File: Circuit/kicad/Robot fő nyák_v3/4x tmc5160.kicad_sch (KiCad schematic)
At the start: 28 parts, among them M6 Stepper_Motor_unipolar_6pin, M7 Stepper_Motor_unipolar_6pin, M8 Stepper_Motor_unipolar_6pin, M9 Stepper_Motor_unipolar_6pin, U42 TMC2240_SILENTSTEPSTICK, U43 TMC2240_SILENTSTEPSTICK, U44 TMC2240_SILENTSTEPSTICK, U45 TMC2240_SILENTSTEPSTICK

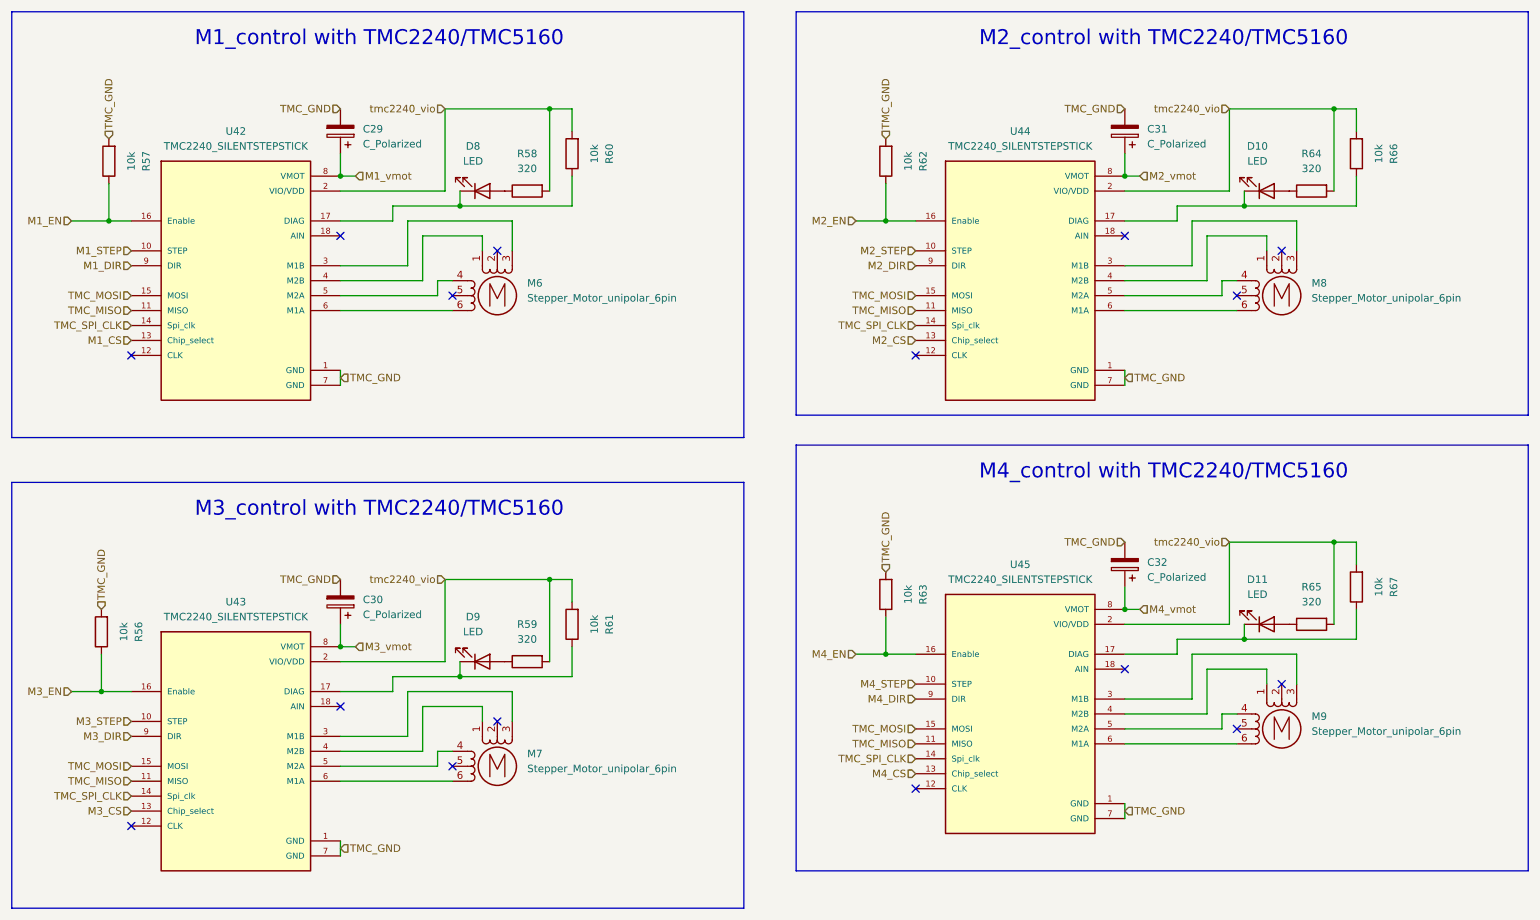
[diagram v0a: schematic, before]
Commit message: kicad i2c schematic updated: gyto i2c bugfixes, +add new datasheets
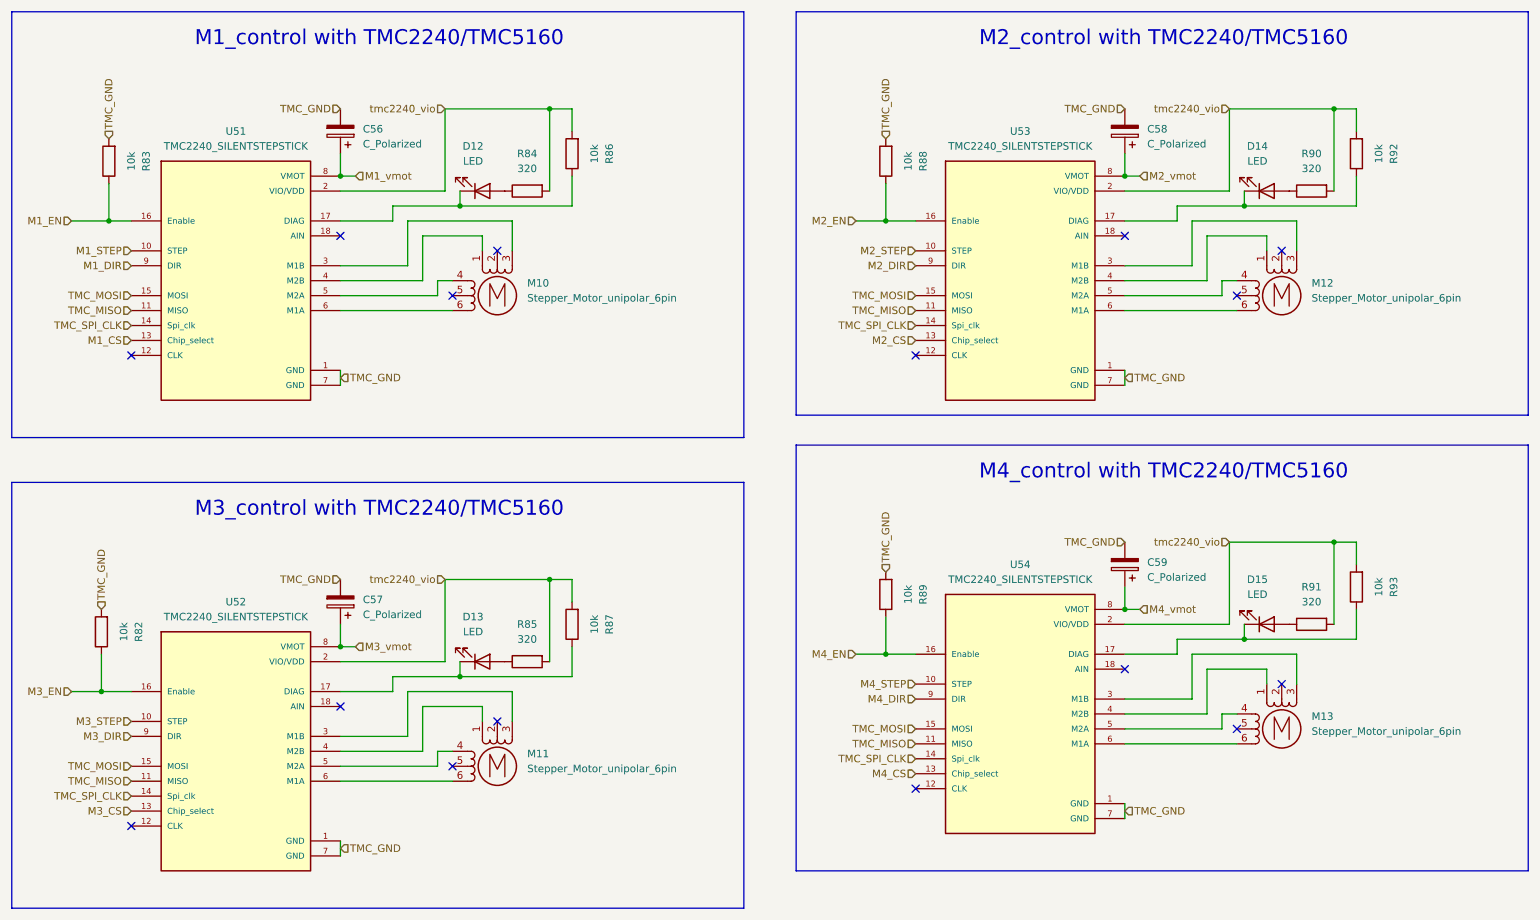
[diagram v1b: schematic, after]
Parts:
- M10: renamed from M6; footprint (none) -> Connector_JST:JST_PH_B6B-PH-K_1x06_P2.00mm_Vertical
- M11: renamed from M7; footprint (none) -> Connector_JST:JST_PH_B6B-PH-K_1x06_P2.00mm_Vertical
- M12: renamed from M8; footprint (none) -> Connector_JST:JST_PH_B6B-PH-K_1x06_P2.00mm_Vertical
- M13: renamed from M9; footprint (none) -> Connector_JST:JST_PH_B6B-PH-K_1x06_P2.00mm_Vertical
- renumbered C29 to C56, C30 to C57, C31 to C58, C32 to C59, D8 to D12, D9 to D13, D10 to D14, D11 to D15, R56 to R82, R57 to R83, R58 to R84, R59 to R85, R60 to R86, R61 to R87, R62 to R88, R63 to R89, R64 to R90, R65 to R91, R66 to R92, R67 to R93, U42 to U51, U43 to U52, U44 to U53, U45 to U54

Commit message: kicad bugfixs + bno085 + level shifter ics
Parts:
- U51: footprint fds:MODULE_TMC2209_SILENTSTEPSTICK -> CM5IO:TMC2209
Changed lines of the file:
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@@
 			)
 		)
-		(property "Footprint" "fds:MODULE_TMC2209_SILENTSTEPSTICK"
+		(property "Footprint" "CM5IO:TMC2209"
 			(at 62.992 27.686 0)
 			(effects

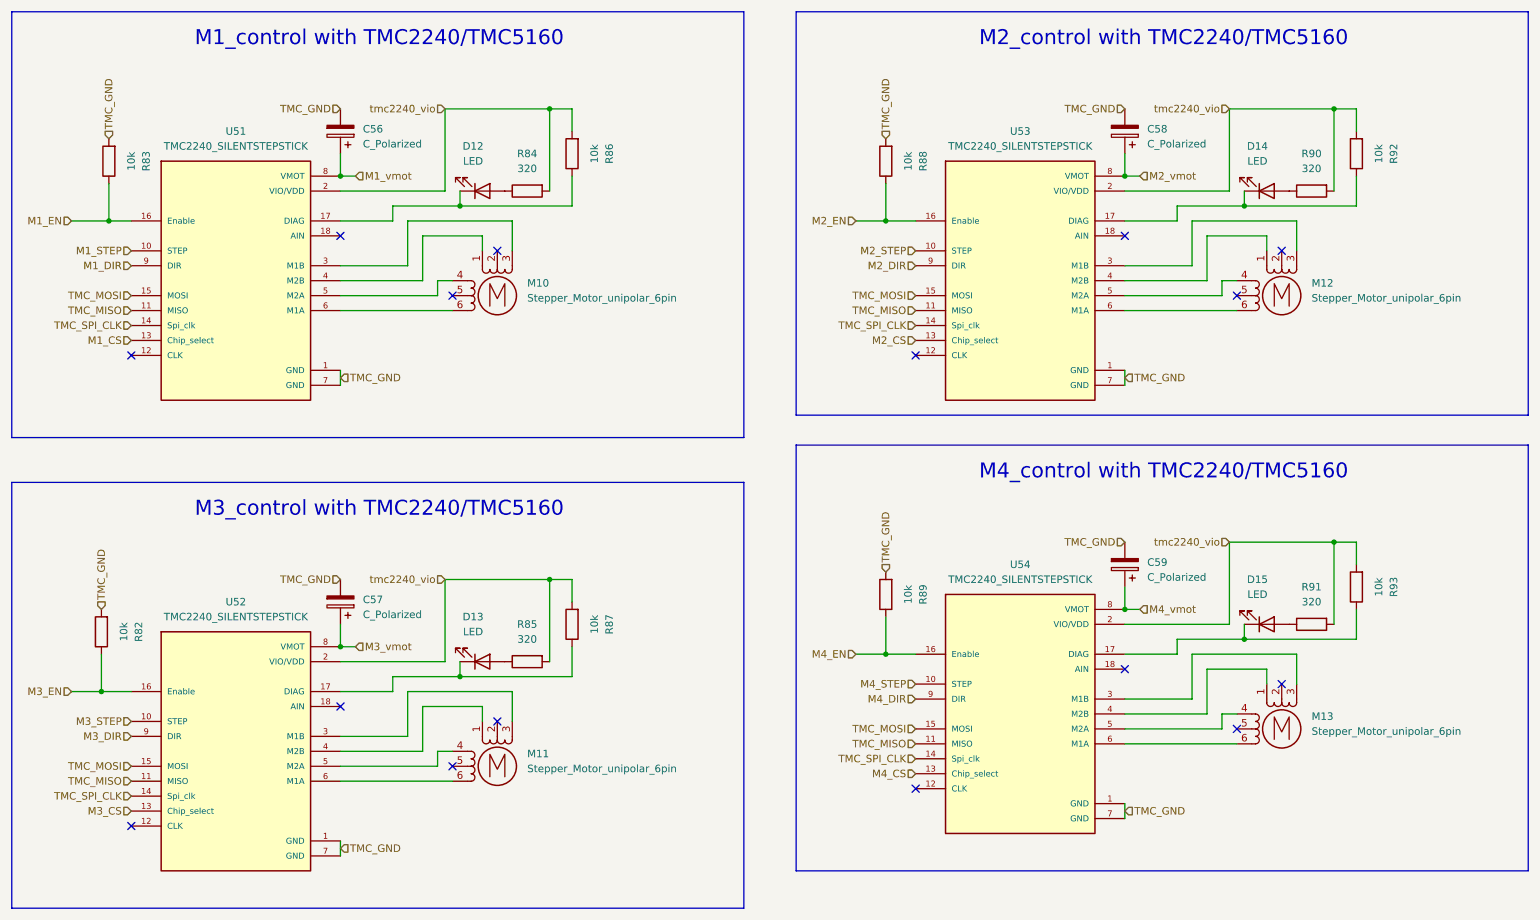
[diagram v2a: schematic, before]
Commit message: KICAD V3.01 Cleaned sheets + update + szekér modell add
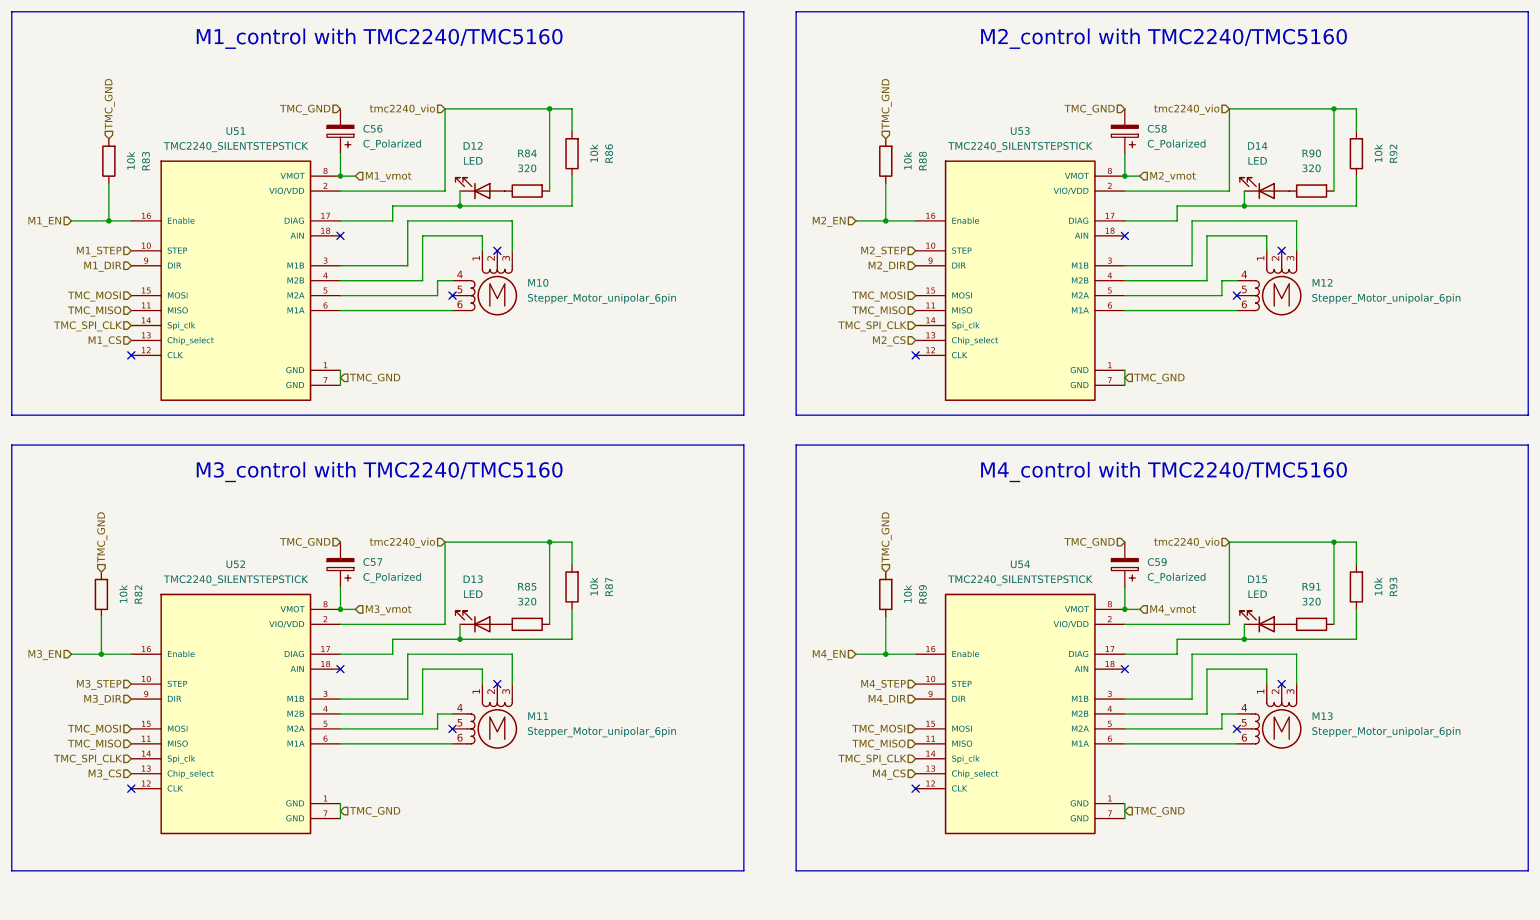
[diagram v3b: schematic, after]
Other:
- moved on the sheet: C57, D13, M11, R82, R85, R87, U52

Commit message: kicad v0.1 footprint- assing spi finish
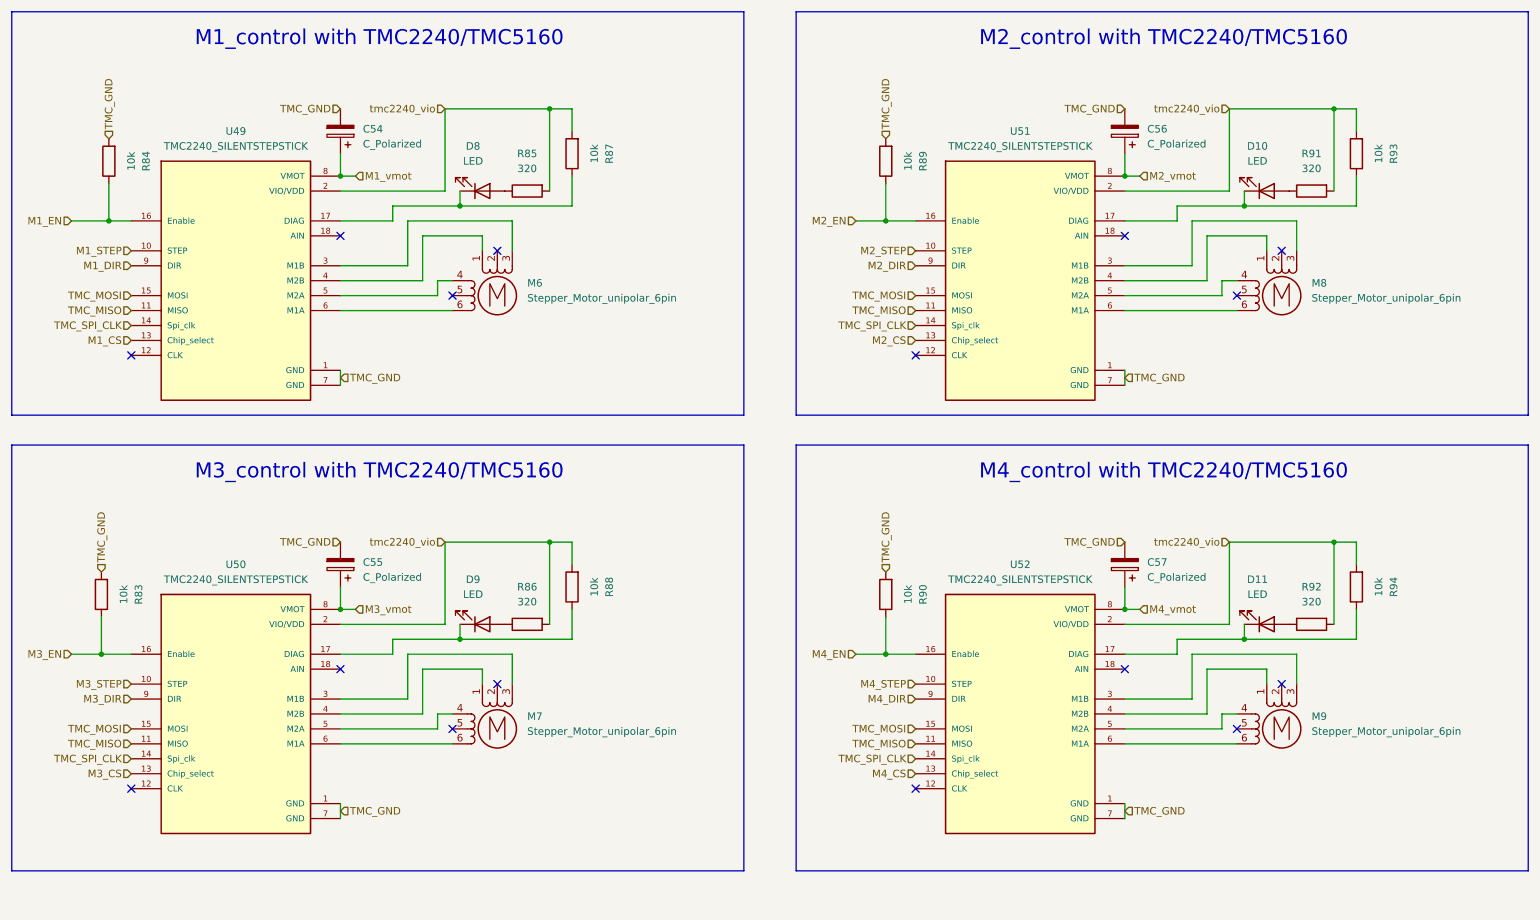
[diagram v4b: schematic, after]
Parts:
- C54: renamed from C56; footprint (none) -> Capacitor_SMD:C_0805_2012Metric
- C55: renamed from C57; footprint (none) -> Capacitor_SMD:C_0805_2012Metric
- C56: renamed from C58; footprint (none) -> Capacitor_SMD:C_0805_2012Metric
- C57: renamed from C59; footprint (none) -> Capacitor_SMD:C_0805_2012Metric
- D10: renamed from D14; footprint (none) -> LED_SMD:LED_0603_1608Metric
- D11: renamed from D15; footprint (none) -> LED_SMD:LED_0603_1608Metric
- D8: renamed from D12; footprint (none) -> LED_SMD:LED_0603_1608Metric
- D9: renamed from D13; footprint (none) -> LED_SMD:LED_0603_1608Metric
- R83: renamed from R82; footprint (none) -> Resistor_SMD:R_0805_2012Metric
- R84: renamed from R83; footprint (none) -> Resistor_SMD:R_0805_2012Metric
- R85: renamed from R84; footprint (none) -> Resistor_SMD:R_0805_2012Metric
- R86: renamed from R85; footprint (none) -> Resistor_SMD:R_0805_2012Metric
- R87: renamed from R86; footprint (none) -> Resistor_SMD:R_0805_2012Metric
- R88: renamed from R87; footprint (none) -> Resistor_SMD:R_0805_2012Metric
- R89: renamed from R88; footprint (none) -> Resistor_SMD:R_0805_2012Metric
- R90: renamed from R89; footprint (none) -> Resistor_SMD:R_0805_2012Metric
- R91: renamed from R90; footprint (none) -> Resistor_SMD:R_0805_2012Metric
- R92: renamed from R91; footprint (none) -> Resistor_SMD:R_0805_2012Metric
- R93: renamed from R92; footprint (none) -> Resistor_SMD:R_0805_2012Metric
- R94: renamed from R93; footprint (none) -> Resistor_SMD:R_0805_2012Metric
- U50: renamed from U52; footprint fds:MODULE_TMC2209_SILENTSTEPSTICK -> CM5IO:TMC2209
- U51: renamed from U53; footprint fds:MODULE_TMC2209_SILENTSTEPSTICK -> CM5IO:TMC2209
- U52: renamed from U54; footprint fds:MODULE_TMC2209_SILENTSTEPSTICK -> CM5IO:TMC2209
- renumbered M10 to M6, M11 to M7, M12 to M8, M13 to M9, U51 to U49

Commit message: kicad update new readme media updates the circuit is 95% finished
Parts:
- C54, C56, C57: value C_Polarized -> 470uf
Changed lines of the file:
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@@
 			)
 		)
-		(property "Value" "C_Polarized"
+		(property "Value" "470uf"
 			(at 212.09 38.9889 0)
 			(effects
@@
 			)
 		)
-		(property "Value" "C_Polarized"
+		(property "Value" "470uf"
 			(at 78.74 38.9889 0)
 			(effects
@@
 			)
 		)
-		(property "Value" "C_Polarized"
+		(property "Value" "470uf"
 			(at 212.09 112.6489 0)
 			(effects
